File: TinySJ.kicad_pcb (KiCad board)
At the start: 2 copper layers, 30 x 20 mm, 6 parts

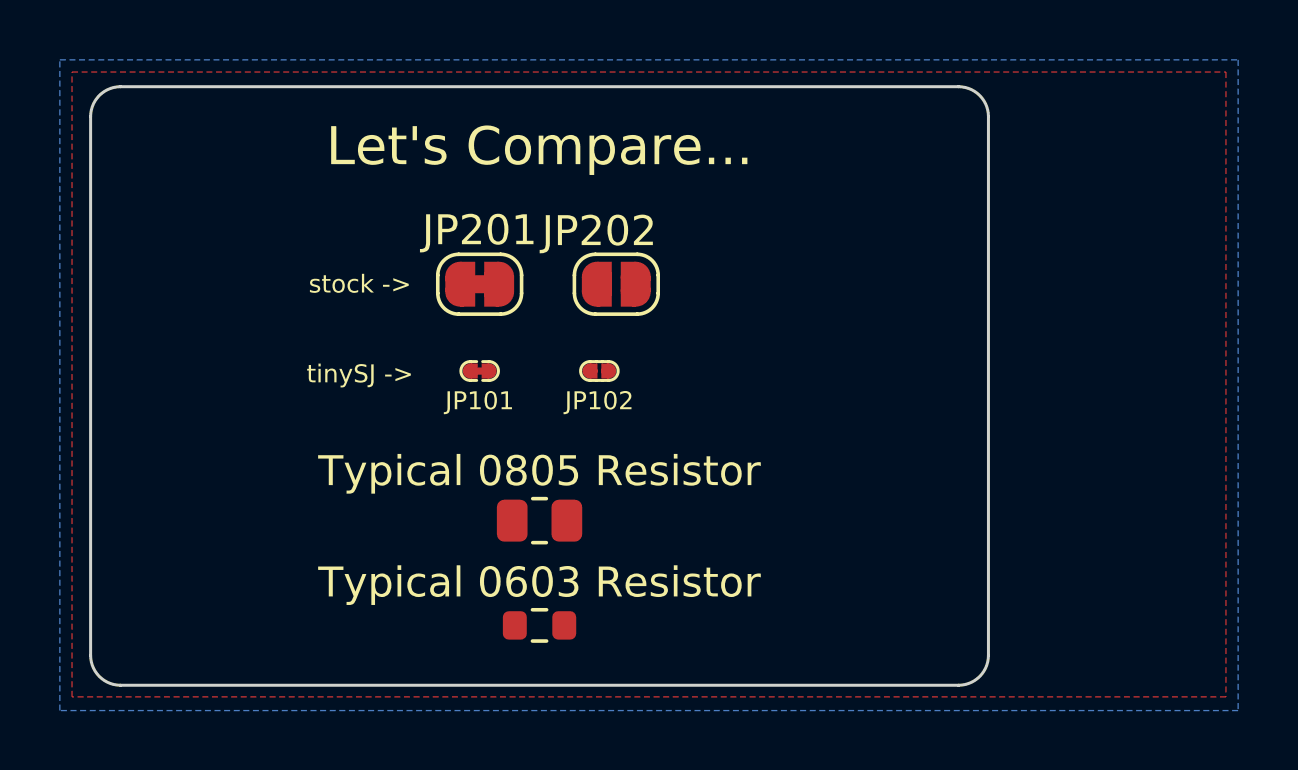
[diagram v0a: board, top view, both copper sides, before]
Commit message: Better tinySJ example board...
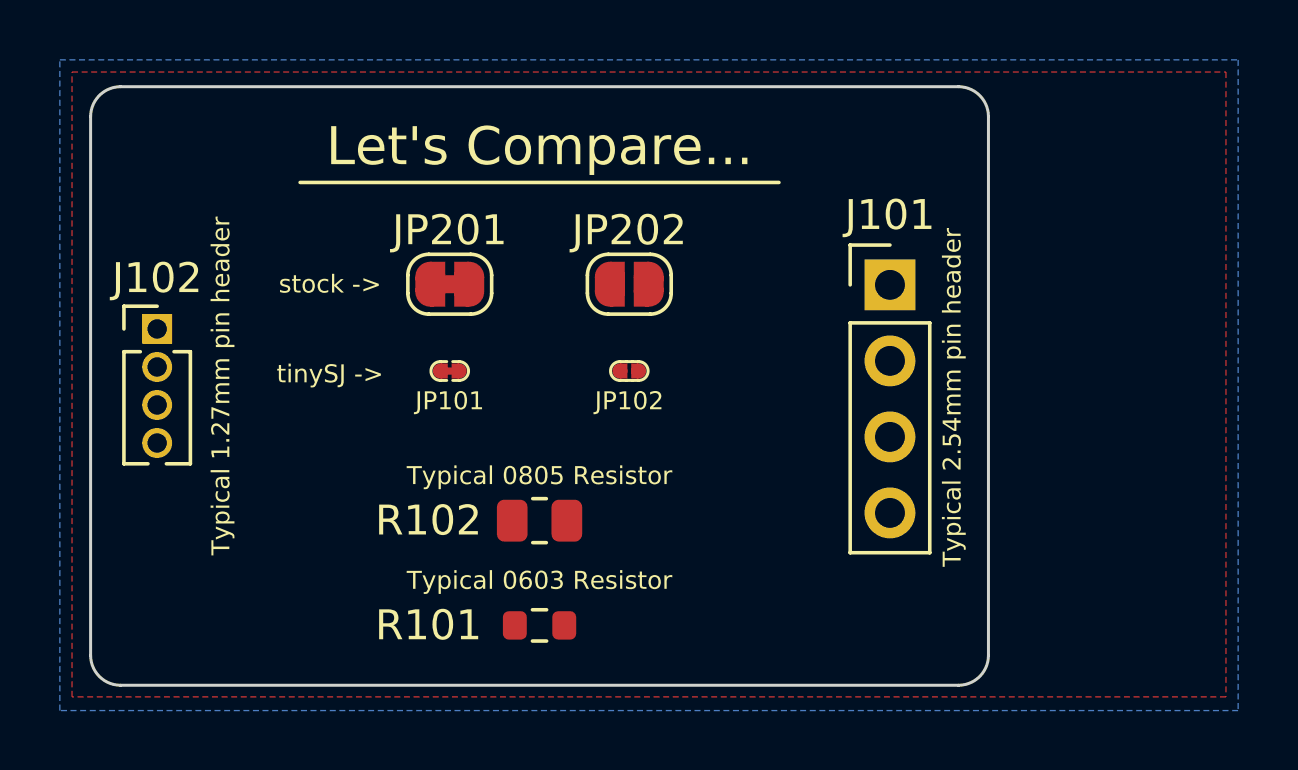
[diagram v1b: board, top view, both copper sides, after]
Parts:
- removed Typical 0603 Resistor: R_0603_1608Metric, Resistor_SMD:R_0603_1608Metric
- removed Typical 0805 Resistor: R_0805_2012Metric, Resistor_SMD:R_0805_2012Metric
- added J101: Conn_01x04_Male, Connector_PinHeader_2.54mm:PinHeader_1x04_P2.54mm_Vertical, F.Cu at (111.7, 96.6)
- added J102: Conn_01x04_Male, Connector_PinHeader_1.27mm:PinHeader_1x04_P1.27mm_Vertical, F.Cu at (87.2, 98.1)
- added R101: R, Resistor_SMD:R_0603_1608Metric, F.Cu at (100.0, 108.0)
- added R102: R, Resistor_SMD:R_0805_2012Metric, F.Cu at (100.0, 104.5)
- moved JP101 1.00 mm to (97.0, 99.5)
- moved JP102 1.00 mm to (103.0, 99.5)
- moved JP201 1.00 mm to (97.0, 96.6)
- moved JP202 0.43 mm to (103.0, 96.6)
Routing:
- added copper zone on B.Cu, net GND
- added copper zone on F.Cu, net Vcc
- removed copper zone on B.Cu, net (none)
- removed copper zone on F.Cu, net (none)
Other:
- board text added: "Typical 0603 Resistor"
- board text added: "Typical 0805 Resistor"
- board text added: "Typical 1.27mm pin header"
- board text added: "Typical 2.54mm pin header"
